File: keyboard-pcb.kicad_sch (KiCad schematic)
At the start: 32 parts, among them J1 Conn_01x04, J3 USB_C_Receptacle_USB2.0_16P, J4 Conn_01x05, SW1 SW_Push, SW2 SW_Push, U1 RP2040, U2 XC6206PxxxMR, U3 W25Q128JVS, U5 SRV05-4, Y1 Crystal_GND24_Small

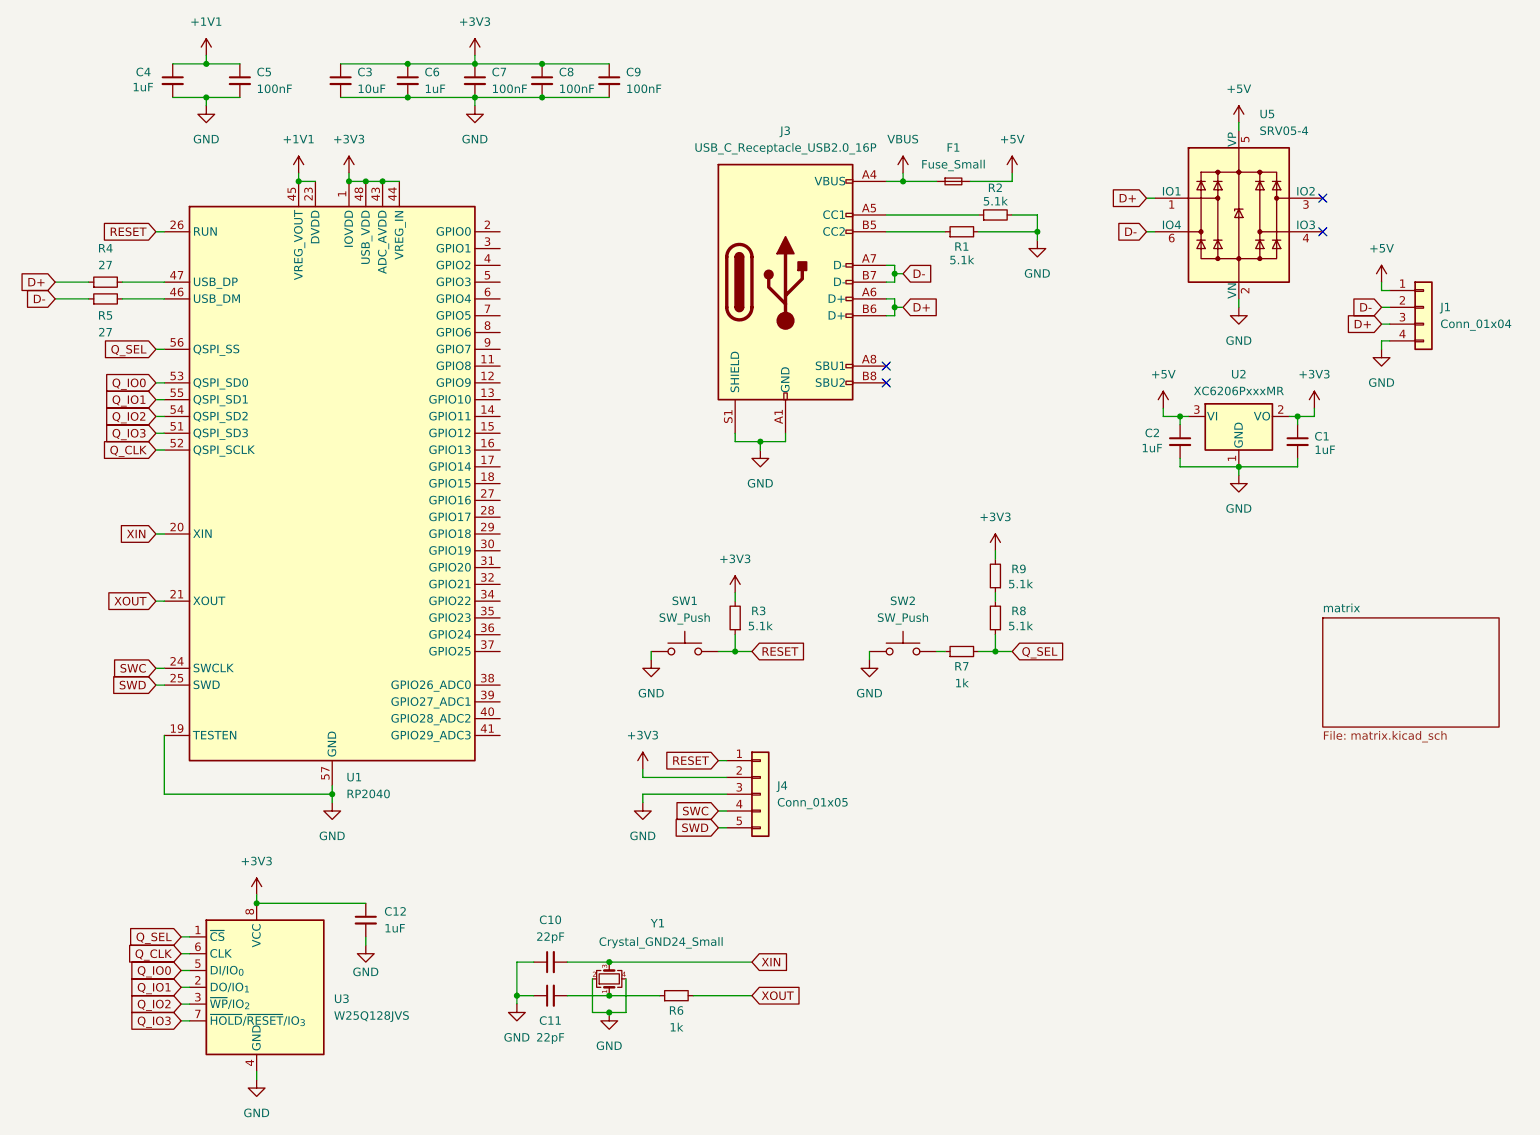
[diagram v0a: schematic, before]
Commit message: Wired MCU loop on PCB
All components of MCU loop wired together, keyswitch matrix remaining
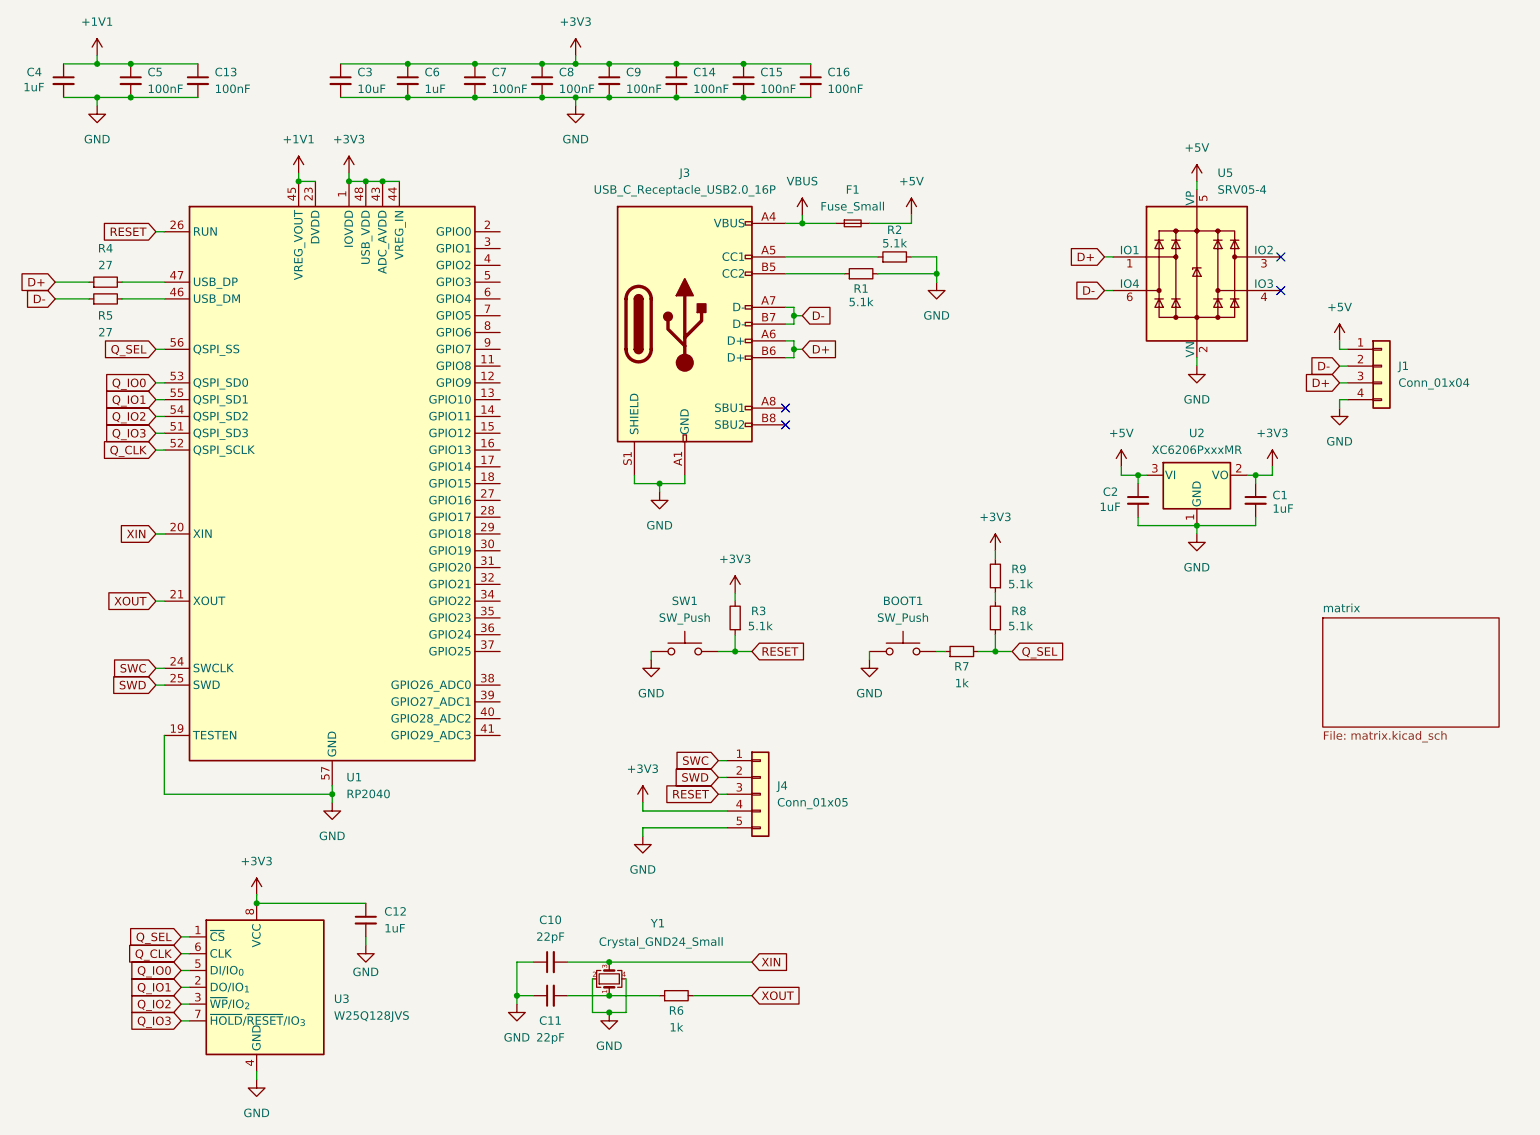
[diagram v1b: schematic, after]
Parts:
- added C13, C14, C15, C16: 100nF, Capacitor_SMD:C_0402_1005Metric, symbol Device:C_Small
- C1, C10, C11, C12, C2, C4, C5, C6, C7, C8, C9: footprint Capacitor_SMD:C_0805_2012Metric -> Capacitor_SMD:C_0402_1005Metric
- C3: footprint Capacitor_SMD:C_0805_2012Metric -> Capacitor_SMD:C_0603_1608Metric
- R1, R2, R3, R4, R5, R6, R7, R8, R9: footprint Resistor_SMD:R_0805_2012Metric -> Resistor_SMD:R_0402_1005Metric
- renumbered SW2 to BOOT1
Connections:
- net +1V1: now also C13.1
- net +3V3: now also J4.4 (Pin_4), C14.1, C15.1, C16.1; no longer J4.2 (Pin_2)
- net GND: now also J4.5 (Pin_5), C13.2, C14.2, C15.2, C16.2; no longer J4.3 (Pin_3)
- net RESET: now also J4.3 (Pin_3); no longer J4.1 (Pin_1)
- net SWC: now also J4.1 (Pin_1); no longer J4.4 (Pin_4)
- net SWD: now also J4.2 (Pin_2); no longer J4.5 (Pin_5)
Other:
- moved on the sheet: C1, C2, C4, C5, F1, J1, J3, R1, R2, U2, U5
